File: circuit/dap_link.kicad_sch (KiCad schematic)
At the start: 32 parts, among them J1 USB_A_CONN, J2 SWD_CONN_5P, J3 UART1_CONN_3P, J5 Conn_02x10_Odd_Even, U1 STM32F103CBTx, U2 AMS1117-3.3, U3 TXS0108EPW, Y1 8MHz

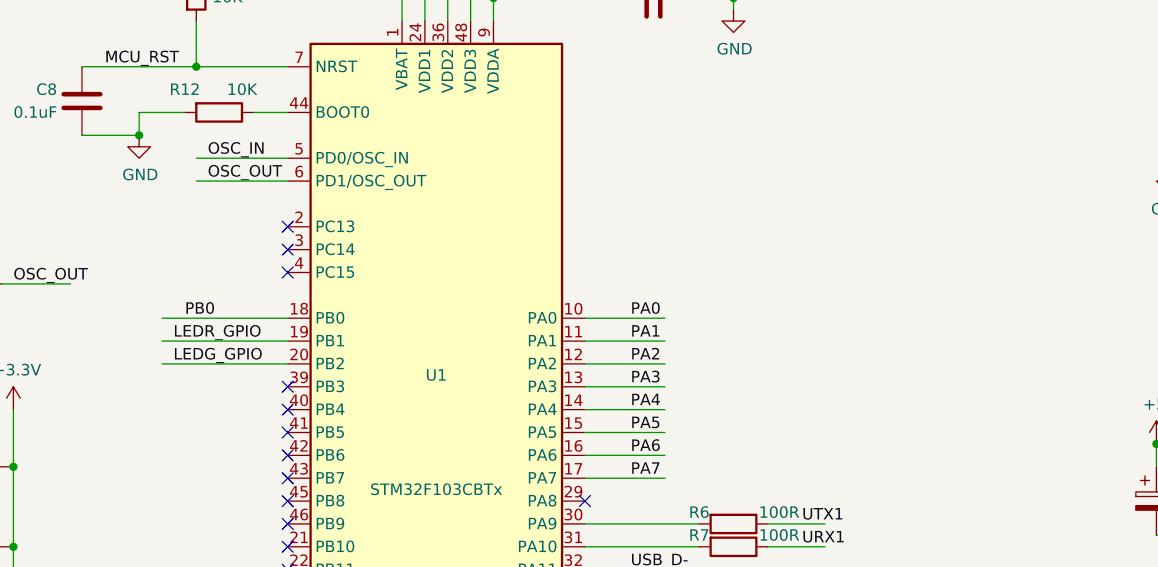
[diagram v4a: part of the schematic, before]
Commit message: 增加boot按钮
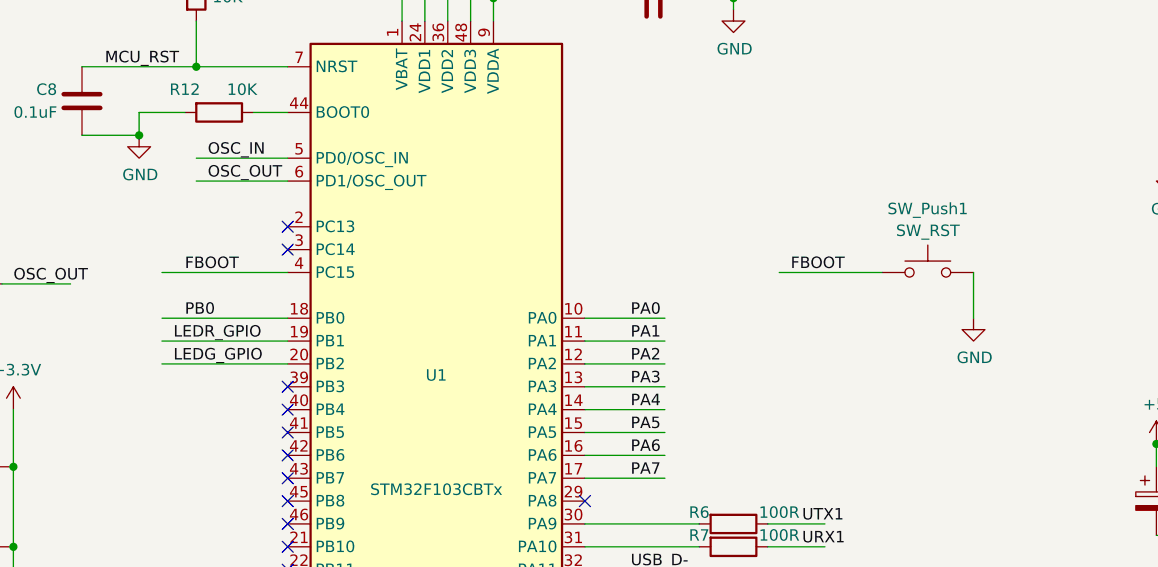
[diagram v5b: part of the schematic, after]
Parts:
- added SW_Push1: SW_RST, Button_Switch_SMD:SW_Push_1P1T_NO_6x6mm_H9.5mm, symbol Switch:SW_Push
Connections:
- net GND: now also SW_Push1.2
- net FBOOT: now reaches U1.4 (PC15)
- net FBOOT: now also SW_Push1.1
- no-connect marks 18 -> 17
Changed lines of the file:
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@@
   (no_connect (at 95.25 92.71))
   (no_connect (at 128.27 100.33))
+  (no_connect (at 95.25 87.63))
   (no_connect (at 95.25 90.17))
-  (no_connect (at 95.25 87.63))
+  (no_connect (at 95.25 105.41))
   (no_connect (at 95.25 97.79))
   (no_connect (at 95.25 95.25))
@@
   (no_connect (at 95.25 110.49))
   (no_connect (at 95.25 69.85))
-  (no_connect (at 95.25 105.41))
   (no_connect (at 95.25 72.39))
   (no_connect (at 95.25 118.11))
-  (no_connect (at 95.25 74.93))
   (wire (pts (xy 220.98 133.35) (xy 228.6 133.35))
     (stroke (width 0) (type default))
@@
     (stroke (width 0) (type default))
   )
+  (wire (pts (xy 81.28 74.93) (xy 95.25 74.93))
+    (stroke (width 0) (type default))
+  )
   (wire (pts (xy 139.7 160.02) (xy 139.7 162.56))
     (stroke (width 0) (type default))
@@
     (stroke (width 0) (type default))
   )
+  (wire (pts (xy 81.28 82.55) (xy 95.25 82.55))
+    (stroke (width 0) (type default))
+  )
   (wire (pts (xy 58.42 133.35) (xy 58.42 138.43))
     (stroke (width 0) (type default))
@@
     (stroke (width 0) (type default))
   )
+  (wire (pts (xy 171.45 74.93) (xy 171.45 80.01))
+    (stroke (width 0) (type default))
+  )
   (wire (pts (xy 85.09 39.37) (xy 85.09 35.56))
     (stroke (width 0) (type default))
@@
     (stroke (width 0) (type default))
   )
-  (wire (pts (xy 81.28 82.55) (xy 95.25 82.55))
-    (stroke (width 0) (type default))
-  )
   (wire (pts (xy 139.7 165.1) (xy 139.7 167.64))
     (stroke (width 0) (type default))
@@
     (stroke (width 0) (type default))
   )
+  (wire (pts (xy 85.09 62.23) (xy 95.25 62.23))
+    (stroke (width 0) (type default))
+  )
+  (wire (pts (xy 118.11 44.45) (xy 118.11 34.29))
+    (stroke (width 0) (type default))
+  )
+  (wire (pts (xy 162.56 138.43) (xy 171.45 138.43))
+    (stroke (width 0) (type default))
+  )
   (wire (pts (xy 81.28 85.09) (xy 95.25 85.09))
     (stroke (width 0) (type default))
   )
-  (wire (pts (xy 85.09 62.23) (xy 95.25 62.23))
-    (stroke (width 0) (type default))
-  )
-  (wire (pts (xy 118.11 44.45) (xy 118.11 34.29))
-    (stroke (width 0) (type default))
-  )
-  (wire (pts (xy 162.56 138.43) (xy 171.45 138.43))
-    (stroke (width 0) (type default))
-  )
   (wire (pts (xy 48.26 68.58) (xy 58.42 68.58))
     (stroke (width 0) (type default))
@@
     (stroke (width 0) (type default))
   )
+  (wire (pts (xy 149.86 74.93) (xy 161.29 74.93))
+    (stroke (width 0) (type default))
+  )
   (wire (pts (xy 33.02 68.58) (xy 33.02 76.2))
     (stroke (width 0) (type default))
@@
     (effects (font (size 1.27 1.27)) (justify left bottom))
   )
+  (label "LEDR_GPIO" (at 82.55 82.55 0) (fields_autoplaced)
+    (effects (font (size 1.27 1.27)) (justify left bottom))
+  )
+  (label "FBOOT" (at 151.13 74.93 0) (fields_autoplaced)
+    (effects (font (size 1.27 1.27)) (justify left bottom))
+  )
   (label "USB_D+" (at 133.35 110.49 0) (fields_autoplaced)
     (effects (font (size 1.27 1.27)) (justify left bottom))
@@
     (effects (font (size 1.27 1.27)) (justify left bottom))
   )
+  (label "FBOOT" (at 83.82 74.93 0) (fields_autoplaced)
+    (effects (font (size 1.27 1.27)) (justify left bottom))
+  )
   (label "PA2" (at 133.35 85.09 0) (fields_autoplaced)
     (effects (font (size 1.27 1.27)) (justify left bottom))
@@
     (effects (font (size 1.27 1.27)) (justify left bottom))
   )
-  (label "LEDR_GPIO" (at 82.55 82.55 0) (fields_autoplaced)
-    (effects (font (size 1.27 1.27)) (justify left bottom))
-  )
   (label "UTX1" (at 152.4 102.87 0) (fields_autoplaced)
     (effects (font (size 1.27 1.27)) (justify left bottom))
@@
     (effects (font (size 1.27 1.27)) (justify left bottom))
   )
+  (label "LEDG_GPIO" (at 82.55 85.09 0) (fields_autoplaced)
+    (effects (font (size 1.27 1.27)) (justify left bottom))
+  )
   (label "VREF" (at 105.41 154.94 0) (fields_autoplaced)
     (effects (font (size 1.27 1.27)) (justify left bottom))
@@
   )
   (label "TCK_SCK" (at 105.41 165.1 0) (fields_autoplaced)
-    (effects (font (size 1.27 1.27)) (justify left bottom))
-  )
-  (label "LEDG_GPIO" (at 82.55 85.09 0) (fields_autoplaced)
     (effects (font (size 1.27 1.27)) (justify left bottom))
   )
@@
         )
       )
+    )
+  )
+  (symbol (lib_id "Switch:SW_Push") (at 166.37 74.93 0) (unit 1)
+    (in_bom yes) (on_board yes) (dnp no) (fields_autoplaced)
+    (property "Reference" "SW_Push1" (at 166.37 67.8647 0)
+      (effects (font (size 1.27 1.27)))
+    )
+    (property "Value" "SW_RST" (at 166.37 70.2889 0)
+      (effects (font (size 1.27 1.27)))
+    )
+    (property "Footprint" "Button_Switch_SMD:SW_Push_1P1T_NO_6x6mm_H9.5mm" (at 166.37 69.85 0)
+      (effects (font (size 1.27 1.27)) hide)
+    )
+    (property "Datasheet" "~" (at 166.37 69.85 0)
+      (effects (font (size 1.27 1.27)) hide)
+    )
+    (pin "1")
+    (pin "2")
+    (instances
+      (project "stm32f302dk"
+        (path "/270d3e73-918a-4e4c-b1ac-c0dced7b5bd0"
+          (reference "SW_Push1") (unit 1)
+        )
+      )
+      (project "dap_link"
+        (path "/9df731a6-2e06-41f7-94bb-21385ffe9471"
+          (reference "SW_Push1") (unit 1)
+        )
+      )
+      (project "nrf52833dk"
+        (path "/d17d0dd2-64bf-4381-9653-c6412fd9bd63"
+          (reference "SW1") (unit 1)
+        )
+      )
+    )
+  )
+  (symbol (lib_id "power:GND") (at 171.45 80.01 0) (unit 1)
+    (in_bom yes) (on_board yes) (dnp no)
+    (property "Reference" "#PWR023" (at 171.45 86.36 0)
+      (effects (font (size 1.27 1.27)) hide)
+    )
+    (property "Value" "GND" (at 171.577 84.4042 0)
+      (effects (font (size 1.27 1.27)))
+    )
+    (property "Footprint" "" (at 171.45 80.01 0)
+      (effects (font (size 1.27 1.27)) hide)
+    )
+    (property "Datasheet" "" (at 171.45 80.01 0)
+      (effects (font (size 1.27 1.27)) hide)
+    )
+    (pin "1")
+    (instances
+      (project "dap_link"
+        (path "/9df731a6-2e06-41f7-94bb-21385ffe9471"
+          (reference "#PWR023") (unit 1)
+        )
+      )

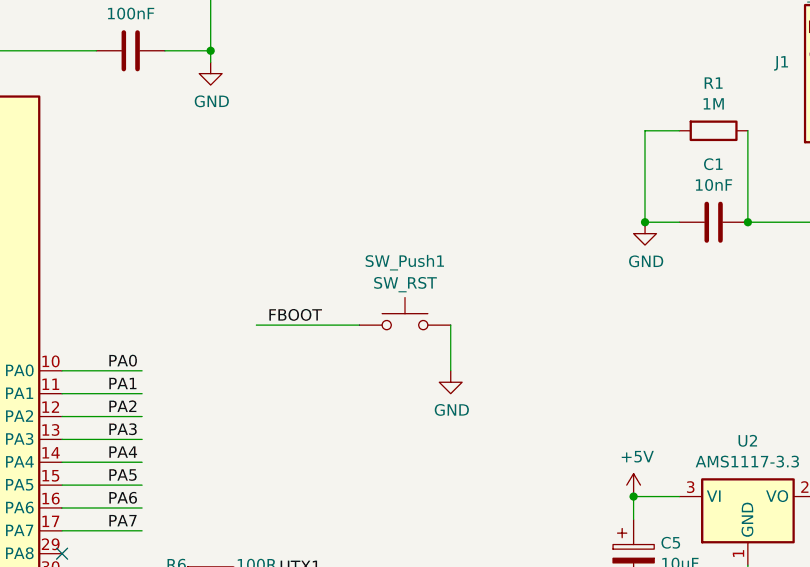
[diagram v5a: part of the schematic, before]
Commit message: 更新丝印
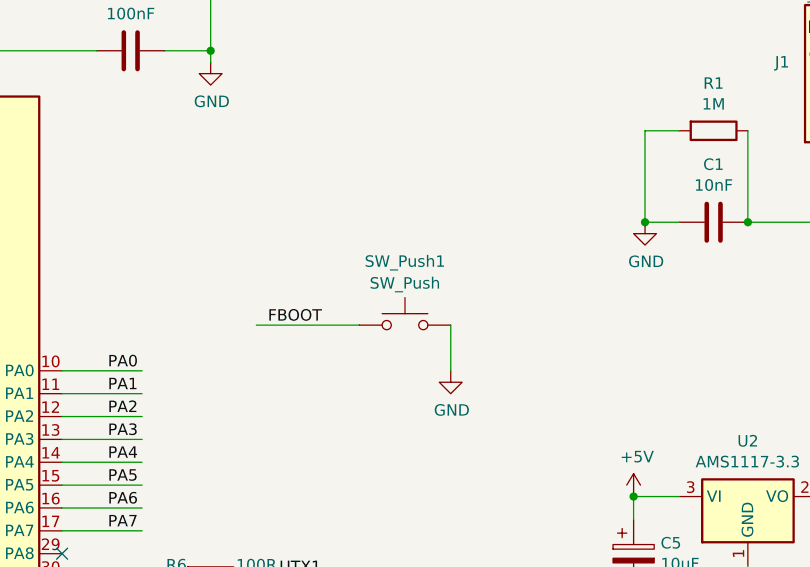
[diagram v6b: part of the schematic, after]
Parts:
- SW_Push1: value SW_RST -> SW_Push
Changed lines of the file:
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@@
       (effects (font (size 1.27 1.27)))
     )
-    (property "Value" "SW_RST" (at 166.37 70.2889 0)
+    (property "Value" "SW_Push" (at 166.37 70.2889 0)
       (effects (font (size 1.27 1.27)))
     )
@@
       (project "dap_link"
         (path "/9df731a6-2e06-41f7-94bb-21385ffe9471"
-          (reference "SW_Push1") (unit 1)
+          (reference "SW1") (unit 1)
         )
       )
